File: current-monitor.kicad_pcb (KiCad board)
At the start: 2 copper layers, 91 parts, among them J103 USB-MICROB, J501 JTAG, U201 AD8429A, U202 LM833, U203 TL032C, U301 INA826, U401 LM27313, U402 LTC3260MSE, U403 MAX6070, U501 K22F-64LQFP, U601 TL032C

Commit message: more layout
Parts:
- added C303: C, libs:SMD-2012, F.Cu at (112.4, 86.0)
- added C304: C, libs:SMD-2012, F.Cu at (116.0, 89.6)
- added C305: C, libs:SMD-2012, F.Cu at (132.8, 88.6)
- added C603: 4n, libs:SMD-2012, F.Cu at (132.8, 79.8)
- added D201: BAS40-04, libs:SOT-23, F.Cu at (128.4, 84.2)
- added D301: BAS40-04, libs:SOT-23, F.Cu at (128.4, 88.6)
- added D601: BAS40-04, libs:SOT-23, F.Cu at (126.8, 79.8)
- added R304: Rs, libs:SMD-1608, F.Cu at (110.4, 88.6)
- added R305: Rs, libs:SMD-1608, F.Cu at (113.4, 88.6)
- added R306: R, libs:SMD-1608, F.Cu at (131.0, 88.4)
- moved R401 131.8 mm to (140.6, 102.0)
- moved R409 129.1 mm to (137.6, 103.6), turned to 270 degrees
- moved R408 127.1 mm to (140.6, 103.6), turned to 270 degrees
- moved C404 122.0 mm to (139.0, 112.6)
- moved C408 122.0 mm to (133.7, 105.4)
- moved C409 122.0 mm to (141.2, 109.6)
- moved C405 122.0 mm to (131.8, 112.6)
- moved C407 122.0 mm to (137.1, 105.4)
- moved C410 122.0 mm to (129.6, 109.6)
- moved R404 122.0 mm to (140.6, 107.0)
- moved R405 122.0 mm to (140.6, 105.4)
- moved R406 122.0 mm to (129.4, 105.4)
- moved R407 122.0 mm to (129.4, 107.0)
- moved R410 122.0 mm to (130.8, 103.6)
- moved U402 122.0 mm to (135.4, 108.6)
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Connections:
- net Net-(C207-Pad2) renamed /Current Sense Fine Range/FINE_UNCLAMPED
- net Net-(R601-Pad1) renamed /Sense Voltage/VOLTAGE_RAW
- U202 pad 5: (no net) -> Net-(C303-Pad1)
- U202 pad 6: (no net) -> /Current Sense Coarse Range/COARSE_UNCLAMPED
- U202 pad 7: (no net) -> /Current Sense Coarse Range/COARSE_UNCLAMPED
- U301 pad 7: /Current Sense Coarse Range/SENSE_COARSE -> Net-(R304-Pad1)
- U501 pad 10: /Current Sense Coarse Range/SENSE_COARSE -> (no net)
- U501 pad 11: /MCU/SENSE_VOLTAGE -> /Current Sense Fine Range/SENSE_FINE
- U501 pad 12: (no net) -> /Current Sense Coarse Range/SENSE_COARSE
- U501 pad 9: /Current Sense Fine Range/SENSE_FINE -> /MCU/SENSE_VOLTAGE
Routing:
- net /Current Sense Fine Range/REF_ADJUST: track 0.00 -> 26.3 mm
- net SENSE+: track 4.63 -> 28.8 mm, vias 1 -> 0
- net /Current Sense Coarse Range/COARSE_UNCLAMPED: track 0.00 -> 18.6 mm
- net COM: track 51.6 -> 68.8 mm, vias 48 -> 66
- net SENSE-: track 4.18 -> 19.6 mm, vias 1 -> 0
- net /Current Sense Fine Range/REF_FINE: track 5.07 -> 20.5 mm
- net /Current Sense Coarse Range/SENSE_COARSE: track 0.00 -> 15.1 mm
- net /MCU/SENSE_VOLTAGE: track 1.60 -> 16.5 mm
- net /Current Sense Fine Range/FINE_UNCLAMPED: track 5.99 -> 20.3 mm
- net /Current Sense Coarse Range/REF_COARSE: track 0.00 -> 13.6 mm
- net +3.00V: track 5.69 -> 18.0 mm
- net Net-(R304-Pad1): track 0.00 -> 10.5 mm
- net /Current Sense Fine Range/SENSE_FINE: track 1.60 -> 11.9 mm
- net Net-(R205-Pad1): track 0.00 -> 10.2 mm
- net +3V3: track 0.00 -> 9.16 mm
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- added copper zone on F.Cu, net +5V
- added copper zone on F.Cu, net /Power Supply/+Vs_UNREG
- added copper zone on F.Cu, net Net-(C402-Pad2)
- added copper zone on F.Cu, net Net-(D401-PadA)

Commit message: more layout
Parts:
- added D101: MMBZ15VALT1G, libs:SOT-23, F.Cu at (84.2, 85.0)
- added Y501: 4MHz, libs:OSC3225, F.Cu at (154.8, 87.4)
- moved S501 91.7 mm to (141.3, 94.3)
- moved J501 74.7 mm to (149.6, 95.2)
- moved R501 63.6 mm to (156.2, 82.8), turned to 270 degrees
- moved C510 63.6 mm to (156.2, 84.4)
- moved C413 23.6 mm to (122.8, 109.0), turned to 270 degrees
- moved C412 22.5 mm to (119.0, 111.4), turned to 0 degrees
- moved U403 20.6 mm to (122.2, 111.4), turned to 270 degrees
- moved C411 17.1 mm to (122.8, 113.8), turned to 270 degrees
- moved C404 10.0 mm to (141.5, 102.9), turned to 90 degrees
- moved C405 9.99 mm to (141.5, 110.1), turned to 90 degrees
- moved R401 9.75 mm to (130.9, 101.3), turned to 180 degrees
- moved C409 9.31 mm to (138.5, 100.7), turned to 180 degrees
- moved C410 9.27 mm to (138.5, 112.3), turned to 180 degrees
- moved C101 9.14 mm to (88.0, 80.6), turned to 180 degrees
- moved C102 9.02 mm to (88.0, 89.4), turned to 0 degrees
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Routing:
- net +5V: track 5.47 -> 67.6 mm, vias 0 -> 5
- net +3.00V: track 18.0 -> 45.5 mm
- net COM: track 68.8 -> 87.5 mm, vias 66 -> 86
- net /MCU/SWD_CLK: track 0.00 -> 17.7 mm
- net /MCU/SWD_DIO: track 0.00 -> 14.7 mm
- net /MCU/UART_TX: track 0.00 -> 12.8 mm
- net /MCU/UART_RX: track 0.00 -> 12.1 mm
- net +3V3: track 9.16 -> 19.6 mm, vias 0 -> 11
- net Net-(C502-Pad1): track 0.00 -> 7.19 mm
- net Net-(C501-Pad1): track 0.00 -> 6.33 mm
- net /MCU/~RESET: track 0.00 -> 5.61 mm
- net Net-(R408-Pad2): track 1.45 -> 2.85 mm
- net /Current Sense Fine Range/REF_ADJUST: track 26.3 -> 27.0 mm, vias 0 -> 2
- added copper zone on In2.Cu, net +3V3
- added copper zone on In2.Cu, net +5V
- added copper zone on In2.Cu, net +Vs
- added copper zone on In2.Cu, net -Vs
- added copper zone on B.Cu, net COM
- added copper zone on F.Cu, net COM
- added copper zone on In1.Cu, net COM
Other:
- board outline added: 100 x 50 mm
- copper layers 2 -> 4
- net class Default: clearance 0.2 -> 0.199
- net class Power: clearance 0.2 -> 0.199
- rule trace_clearance: 0.2 -> 0.199

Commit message: more layout
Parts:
- added C511: 1u, libs:SMD-2012, F.Cu at (135.8, 86.2)
- added R502: 33, libs:SMD-1608, F.Cu at (143.4, 72.2)
- added R503: 33, libs:SMD-1608, F.Cu at (143.4, 73.8)
- moved R401 17.3 mm to (148.2, 100.8), turned to 90 degrees
- moved FB501 2.00 mm to (136.0, 88.0)
- moved S501 1.03 mm to (140.8, 95.2)
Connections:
- S501 pad 1: COM -> (no net)
- S501 pad 2: (no net) -> COM
- S501 pad 3: /MCU/~RESET -> (no net)
- S501 pad 4: (no net) -> /MCU/~RESET
- U501 pad 5: /MCU/USB_DP -> Net-(R502-Pad2)
- U501 pad 6: /MCU/USB_DM -> Net-(R503-Pad2)
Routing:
- net /MCU/VS_ENABLE: track 3.17 -> 50.7 mm, vias 2 -> 5
- net /MCU/USB_DM: track 0.00 -> 40.4 mm
- net /MCU/USB_DP: track 0.00 -> 40.3 mm
- net /MCU/~RESET: track 5.61 -> 25.1 mm, vias 0 -> 3
- net +3.00V: track 45.5 -> 60.0 mm
- net /Power Supply/+Vs_UNREG: track 3.32 -> 16.4 mm
- net Net-(R502-Pad2): track 0.00 -> 9.24 mm
- net Net-(R503-Pad2): track 0.00 -> 8.18 mm
- net Net-(R408-Pad2): track 2.85 -> 8.91 mm, vias 1 -> 3
- net Net-(R410-Pad1): track 1.94 -> 5.20 mm, vias 1 -> 2
- net COM: track 87.5 -> 90.7 mm, vias 86 -> 89
- net Net-(C504-Pad1): track 4.86 -> 6.86 mm
- net +3V3: track 19.6 -> 21.6 mm, vias 11 -> 13

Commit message: renumber pcb
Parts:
- added K201: RELAY-DPDT-EE2-SPLIT, libs:RELAY-EE2-NU, F.Cu at (82.0, 143.0)
- added K202: RELAY-DPDT-EE2-SPLIT, libs:RELAY-EE2-NU, F.Cu at (82.0, 132.0)
- added K203: RELAY-DPDT-EE2-SPLIT, libs:RELAY-EE2-NU, F.Cu at (82.0, 165.0)
- added K204: RELAY-DPDT-EE2-SPLIT, libs:RELAY-EE2-NU, F.Cu at (82.0, 154.0)
- added Q201: DRDC3105E6, libs:SOT-23-6, F.Cu at (106.0, 135.0)
- added Q202: DRDC3105E6, libs:SOT-23-6, F.Cu at (102.0, 135.0)
- added Q203: NMOS, libs:SOT-23-FET, F.Cu at (149.7, 148.7)
- added Q204: NMOS, libs:SOT-23-FET, F.Cu at (157.6, 148.7)
- added Q205: NMOS, libs:SOT-23-FET, F.Cu at (153.7, 148.7)
- added R202: 470k 0.05%, libs:SMD-1608, F.Cu at (172.9, 138.2)
- added R203: 470k 0.05%, libs:SMD-1608, F.Cu at (154.0, 154.0)
- added R204: 470k 0.05%, libs:SMD-1608, F.Cu at (172.9, 131.4)
- added R205: Rs, libs:SMD-1608, F.Cu at (153.4, 140.5)
- added R206: 16k 0.05%, libs:SMD-1608, F.Cu at (156.0, 154.0)
- added R207: Rs, libs:SMD-1608, F.Cu at (156.6, 140.8)
- added R208: 150 0.05%, libs:SMD-1608, F.Cu at (152.0, 154.0)
- added R209: Rs, libs:SMD-1608, F.Cu at (150.2, 140.5)
- moved R601 1.60 mm to (143.4, 73.8)
- moved R602 1.60 mm to (143.4, 72.2)
- renumbered C102 to C201, C101 to C202, C201 to C301, C202 to C302, C203 to C303, C204 to C304, C205 to C305, C206 to C306, C212 to C307, C207 to C308, C208 to C309, C209 to C310, C215 to C311, C210 to C312, C301 to C401, C302 to C402, C303 to C403, C304 to C404, C213 to C405, C214 to C406, C306 to C407, C305 to C408, C601 to C501, C602 to C502, C603 to C503, C501 to C601, C502 to C602, C511 to C603, C503 to C604, C504 to C605, C505 to C606, C506 to C607, C507 to C608, C508 to C609, C510 to C610, C509 to C611, C401 to C701, C411 to C702, C412 to C703, C402 to C704, C413 to C705, C403 to C706, C404 to C707, C405 to C708, C406 to C709, C407 to C710, C408 to C711, C409 to C712, C410 to C713, D101 to D201, D201 to D301, D301 to D401, D601 to D501, D401 to D701, FB501 to FB601, J103 to J601, J501 to J602, L401 to L701, R101 to R201, R201 to R301, R202 to R302, R203 to R303, R204 to R304, R205 to R305, R206 to R306, R210 to R307, R211 to R308, R207 to R309, R208 to R310, R212 to R311, R213 to R312, R209 to R313, R301 to R401, R304 to R402, R305 to R403, R302 to R404, R303 to R405, R306 to R406, R603 to R501, R604 to R502, R601 to R503, R602 to R504, R502 to R601, R503 to R602, R501 to R603, R401 to R701, R402 to R702, R403 to R703, R408 to R704, R409 to R705, R410 to R706, R404 to R707, R405 to R708, R406 to R709, R407 to R710, S501 to S601, U201 to U301, U203 to U302, U202 to U303, U301 to U401, U601 to U501, U501 to U601, U401 to U701, U403 to U702, U402 to U703, Y501 to Y601
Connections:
- net Net-(C402-Pad2) renamed /Power Supply/DC_FB
- net Net-(C406-Pad1) renamed /Power Supply/PUMP+
- net Net-(C406-Pad2) renamed /Power Supply/PUMP-
- net Net-(D401-PadA) renamed /Power Supply/DC_SW
- C201 pad 1: SENSE+ -> Net-(C201-Pad1)
- C202 pad 1: SENSE- -> Net-(C202-Pad1)
- D201 pad 1: SENSE+ -> Net-(C201-Pad1)
- D201 pad 2: SENSE- -> Net-(C202-Pad1)
- R601 pad 1: /MCU/USB_DP -> /MCU/USB_DM
- R601 pad 2: Net-(R502-Pad2) (its old number) -> Net-(R601-Pad2)
- R602 pad 1: /MCU/USB_DM -> /MCU/USB_DP
- R602 pad 2: Net-(R503-Pad2) -> Net-(R602-Pad2)
- U601 pad 5: Net-(R502-Pad2) (its old number) -> Net-(R602-Pad2)
- U601 pad 50: (no net) -> /In/Out, Shunt, Calibration/RELAY_INOUT_SHORT
- U601 pad 51: (no net) -> /In/Out, Shunt, Calibration/RELAY_CALIBRATE
- U601 pad 52: (no net) -> /In/Out, Shunt, Calibration/CALIBRATE_5V
- U601 pad 53: (no net) -> /In/Out, Shunt, Calibration/CALIBRATE_3V
- U601 pad 54: (no net) -> /In/Out, Shunt, Calibration/CALIBRATE_30mA
- U601 pad 55: (no net) -> /In/Out, Shunt, Calibration/CALIBRATE_300uA
- U601 pad 56: (no net) -> /In/Out, Shunt, Calibration/CALIBRATE_3uA
- U601 pad 6: Net-(R503-Pad2) -> Net-(R601-Pad2)
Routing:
- net Net-(R602-Pad2): track 0.00 -> 9.24 mm
- net Net-(R502-Pad2) (its old number): track 9.24 -> 0.00 mm
- net Net-(R601-Pad2): track 0.00 -> 8.18 mm
- net Net-(R503-Pad2): track 8.18 -> 0.00 mm
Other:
- board size 100 x 50 mm -> 100 x 70 mm

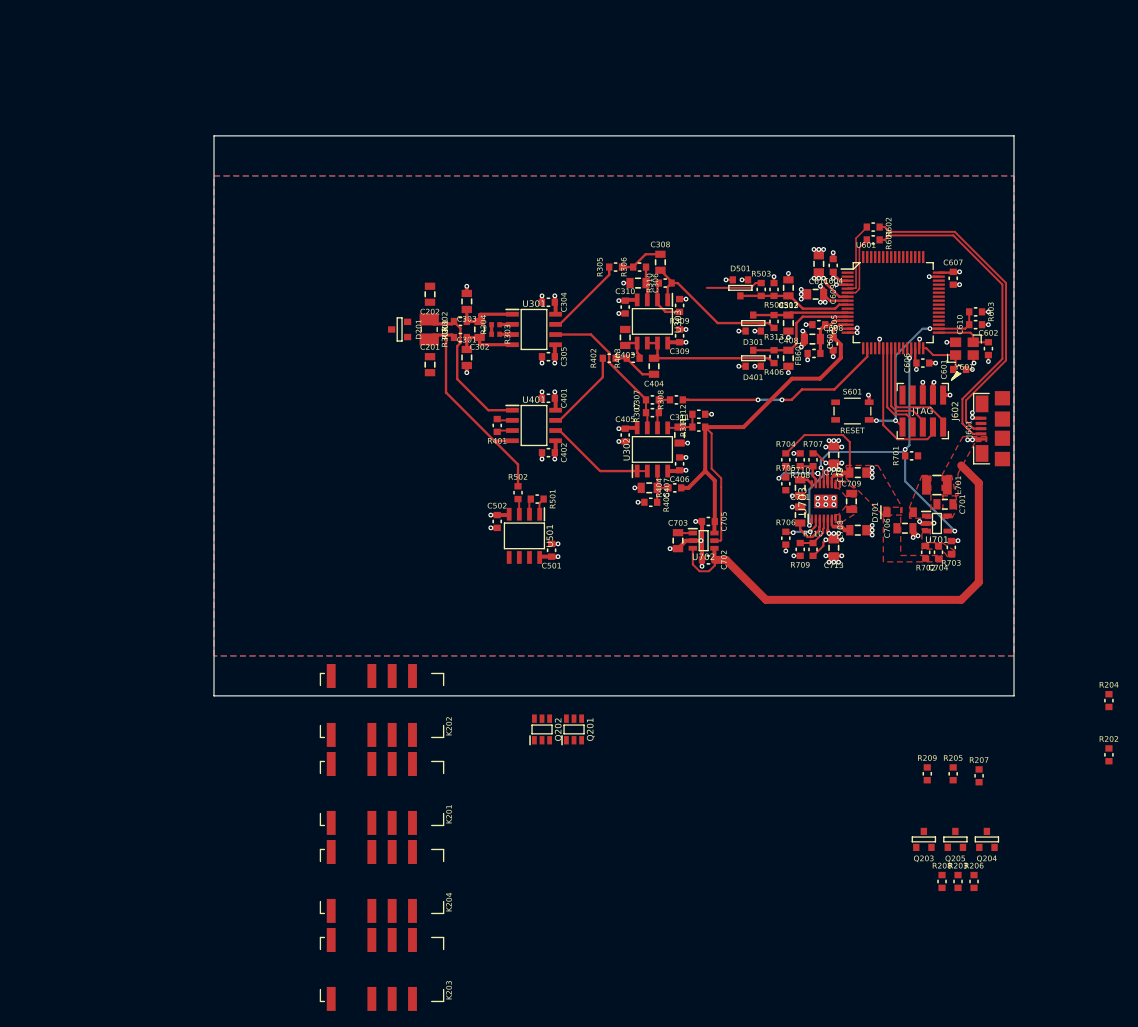
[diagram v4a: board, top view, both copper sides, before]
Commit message: use screw terminals
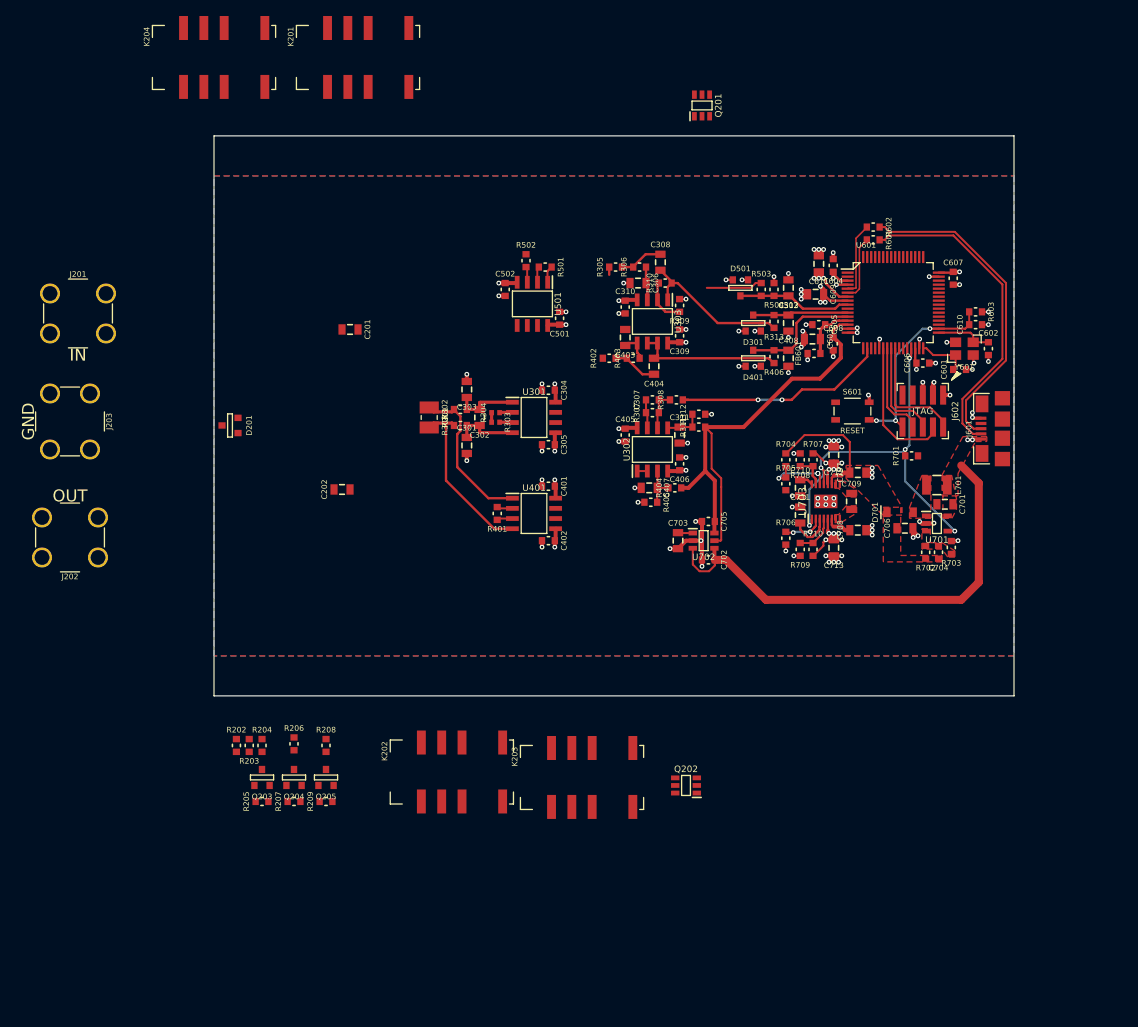
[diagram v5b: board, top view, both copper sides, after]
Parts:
- added J201: IN, libs:SCREW-TERMINAL-7050, F.Cu at (44.0, 83.0)
- added J202: OUT, libs:SCREW-TERMINAL-7050, F.Cu at (43.0, 111.0)
- added J203: GND, libs:SCREW-TERMINAL-7050, F.Cu at (43.0, 96.5)
- moved R202 109.1 mm to (63.8, 137.0)
- moved R204 106.0 mm to (67.0, 137.0)
- moved K204 105.1 mm to (61.0, 51.0), turned to 180 degrees
- moved K201 92.0 mm to (79.0, 51.0), turned to 180 degrees
- moved R203 90.2 mm to (65.4, 137.0), turned to 180 degrees
- moved Q204 87.0 mm to (71.0, 141.0)
- moved R206 86.7 mm to (71.0, 136.8)
- moved R205 86.5 mm to (67.0, 144.0), turned to 90 degrees
- moved R207 85.7 mm to (71.0, 144.0), turned to 90 degrees
- moved Q203 83.1 mm to (67.0, 141.0)
- moved Q201 79.6 mm to (122.0, 57.0)
- moved Q205 79.1 mm to (75.0, 141.0)
- moved R208 78.9 mm to (75.0, 137.0)
- moved R209 75.2 mm to (75.0, 144.0), turned to 90 degrees
- moved K203 34.7 mm to (107.0, 141.0), turned to 180 degrees
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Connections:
- net Net-(C201-Pad1) renamed /In/Out, Shunt, Calibration/IN
- C202 pad 1: Net-(C202-Pad1) -> /In/Out, Shunt, Calibration/OUT
- D201 pad 2: Net-(C202-Pad1) -> /In/Out, Shunt, Calibration/OUT
- K201 pad 5: Net-(C202-Pad1) -> /In/Out, Shunt, Calibration/OUT
- K202 pad 4: +5V -> (no net)
- K202 pad 5: Net-(K202-Pad5) -> (no net)
- K202 pad 8: (no net) -> Net-(K202-Pad8)
- K202 pad 9: (no net) -> +5V
- K203 pad 4: +3.00V -> (no net)
- K203 pad 5: Net-(K202-Pad5) -> (no net)
- K203 pad 8: (no net) -> Net-(K202-Pad8)
- K203 pad 9: (no net) -> +3.00V
- K204 pad 10: Net-(K204-Pad10) -> /In/Out, Shunt, Calibration/OUT
- K204 pad 5: Net-(K202-Pad5) -> Net-(K202-Pad8)
- K204 pad 8: Net-(C202-Pad1) -> Net-(K204-Pad8)
- R202 pad 1: Net-(K204-Pad10) -> Net-(K204-Pad8)
- R206 pad 1: Net-(K204-Pad10) -> Net-(K204-Pad8)
- R208 pad 1: Net-(K204-Pad10) -> Net-(K204-Pad8)
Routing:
- net /Current Sense Fine Range/REF_FINE: track 20.5 -> 5.12 mm
- net /Current Sense Coarse Range/REF_COARSE: track 13.6 -> 1.77 mm
- net Net-(R402-Pad1): track 10.5 -> 0.50 mm
- net Net-(R305-Pad1): track 10.2 -> 1.47 mm
- net SENSE+: track 28.8 -> 21.9 mm

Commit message: checkpoint
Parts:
- removed FB601: FERRITE, libs:SMD-1608
- removed J202: OUT, libs:SCREW-TERMINAL-7050
- removed J203: GND, libs:SCREW-TERMINAL-7050
- removed the K202 at (90.7, 140.3)
- removed K203: RELAY-DPDT-EE2-SPLIT, libs:RELAY-EE2-NU
- removed Q202: DRDC3105E6, libs:SOT-23-6
- removed Q203, Q204, Q205: NMOS, libs:SOT-23-FET
- removed the R205 at (67.0, 144.0)
- removed R209: Rs, libs:SMD-1608
- added C203: 0.1u, libs:SMD-1608, F.Cu at (138.0, 65.4)
- added C204: 0.1u, libs:SMD-1608, F.Cu at (146.6, 71.6)
- added D601: POWER, libs:SMD-1608-LED, F.Cu at (93.8, 79.0)
- added D602: ERROR, libs:SMD-1608-LED, F.Cu at (93.8, 89.0)
- added D603: CAPTURE, libs:SMD-1608-LED, F.Cu at (93.8, 99.0)
- added D604: CALIBRATE, libs:SMD-1608-LED, F.Cu at (93.8, 109.0)
- added F201: FUSE, libs:SMD-1608, F.Cu at (100.6, 63.0)
- added J603: CONN-6, libs:CONN-6-2.54-1.0-PTH, F.Cu at (157.6, 72.5)
- added L601: LCORE, libs:SMD-1608, F.Cu at (136.0, 88.0)
- added L702: LCORE, libs:SMD-1608, F.Cu at (134.2, 97.8)
- added R208: 470k, libs:SMD-1608, F.Cu at (106.0, 76.2)
- added R604: 1k, libs:SMD-1608, F.Cu at (93.8, 82.0)
- added R605: 1k, libs:SMD-1608, F.Cu at (93.8, 92.0)
- added R606: 1k, libs:SMD-1608, F.Cu at (93.8, 102.0)
- added R607: 1k, libs:SMD-1608, F.Cu at (93.8, 112.0)
- added SJ601: SENSE_MCU, libs:SMD-2012, F.Cu at (153.6, 100.0)
- added SJ701: SENSE_ANALOG, libs:SMD-2012, F.Cu at (156.6, 103.6)
- added TP201: SENSE+, libs:TESTPOINT-2.0, F.Cu at (97.8, 82.0)
- added TP202: SENSE-, libs:TESTPOINT-2.0, F.Cu at (107.8, 86.2)
- added TP301: REF_FINE, libs:TESTPOINT-2.0, F.Cu at (123.2, 101.4)
- added TP302: FINE_LOW, libs:TESTPOINT-2.0, F.Cu at (108.4, 99.8)
- added TP303: FINE_UNCLAMPED, libs:TESTPOINT-2.0, F.Cu at (122.2, 85.6)
- added TP304: REF_ADJUST, libs:TESTPOINT-2.0, F.Cu at (141.0, 90.2)
- added TP305: FINE, libs:TESTPOINT-2.0, F.Cu at (125.2, 83.2)
- added TP401: REF_COARSE, libs:TESTPOINT-2.0, F.Cu at (120.8, 114.0)
- added TP402: COARSE_LOW, libs:TESTPOINT-2.0, F.Cu at (108.6, 105.0)
- added TP403: COARSE_UNCLAMPED, libs:TESTPOINT-2.0, F.Cu at (123.4, 95.6)
- added TP404: COARSE, libs:TESTPOINT-2.0, F.Cu at (124.0, 90.4)
- added TP501: VOLTAGE_RAW, libs:TESTPOINT-2.0, F.Cu at (125.0, 75.6)
- added TP502: VOLTAGE, libs:TESTPOINT-2.0, F.Cu at (121.6, 80.4)
- added TP701: +3.00V, libs:TESTPOINT-2.0, F.Cu at (136.6, 96.2)
- added TP702: +Vs_UNREG, libs:TESTPOINT-2.0, F.Cu at (145.4, 102.0)
- added TP703: -Vs_UNREG, libs:TESTPOINT-2.0, F.Cu at (145.8, 114.8)
- added TP704: +Vs, libs:TESTPOINT-2.0, F.Cu at (119.0, 105.4)
- added TP705: -Vs, libs:TESTPOINT-2.0, F.Cu at (98.0, 104.2)
- added U201: FSA1259A, libs:VFSOP-8, F.Cu at (138.6, 63.4)
- added U202: MAX4737EUD, libs:TSSOP-14, F.Cu at (148.8, 68.0)
- J201: value IN -> CONN-3; footprint libs:SCREW-TERMINAL-7050 -> libs:TERM-3-3.5-PTH
- R207: value Rs -> 470k
- moved R206 105.4 mm to (151.4, 64.4), turned to 90 degrees
- moved R202 102.8 mm to (142.8, 71.2), turned to 90 degrees
- moved R203 102.6 mm to (142.8, 69.6), turned to 270 degrees
- moved R204 102.5 mm to (142.8, 68.0), turned to 90 degrees
- moved R205 100.8 mm to (142.8, 66.0), turned to 90 degrees
- moved R207 79.4 mm to (116.4, 78.8), turned to 0 degrees
- moved D201 70.9 mm to (130.3, 75.0), turned to 180 degrees
- moved J201 57.1 mm to (99.8, 71.0), turned to 270 degrees
- moved K201 53.5 mm to (111.9, 67.6), turned to 0 degrees
- moved K202 51.6 mm to (127.9, 67.6), turned to 0 degrees
- moved C202 42.2 mm to (107.8, 76.2), turned to 0 degrees
- moved C201 37.1 mm to (114.6, 78.8), turned to 0 degrees
- moved R502 30.8 mm to (112.4, 104.6), turned to 90 degrees
- moved C501 30.3 mm to (117.2, 111.0)
- moved C502 30.3 mm to (110.4, 107.4)
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- renumbered K204 to K201, K201 to K202, R206 to R205, R208 to R206
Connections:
- net Net-(R402-Pad1) renamed /Current Sense Coarse Range/COARSE_UNFILTERED
- C609 pad 1: +5V -> /MCU/5V_MCU
- C701 pad 1: +5V -> /Power Supply/5V_ANALOG
- C702 pad 1: +5V -> Net-(C702-Pad1)
- J201 pad 1: /In/Out, Shunt, Calibration/IN -> Net-(F201-Pad2)
- K202 pad 4: /In/Out, Shunt, Calibration/IN -> (no net)
- K202 pad 5: /In/Out, Shunt, Calibration/OUT -> (no net)
- K202 pad 8: (no net) -> /In/Out, Shunt, Calibration/IN
- K202 pad 9: (no net) -> /In/Out, Shunt, Calibration/OUT
- L701 pad 1: +5V -> /Power Supply/5V_ANALOG
- R207 pad 1: /In/Out, Shunt, Calibration/CALIBRATE_300uA -> /In/Out, Shunt, Calibration/IN
- U501 pad 5: (no net) -> COM
- U501 pad 6: (no net) -> Net-(U501-Pad6)
- U501 pad 7: (no net) -> Net-(U501-Pad6)
- U601 pad 43: (no net) -> /MCU/GPIO0
- U601 pad 44: (no net) -> /MCU/GPIO1
- U601 pad 45: (no net) -> /MCU/GPIO2
- U601 pad 46: (no net) -> /MCU/GPIO3
- U601 pad 49: (no net) -> /MCU/GPIO4
- U601 pad 50: /In/Out, Shunt, Calibration/RELAY_INOUT_SHORT -> (no net)
- U601 pad 51: /In/Out, Shunt, Calibration/RELAY_CALIBRATE -> (no net)
- U601 pad 52: /In/Out, Shunt, Calibration/CALIBRATE_5V -> (no net)
- U601 pad 53: /In/Out, Shunt, Calibration/CALIBRATE_3V -> /MCU/LED_CALIBRATE
- U601 pad 54: /In/Out, Shunt, Calibration/CALIBRATE_30mA -> /MCU/LED_CAPTURE
- U601 pad 55: /In/Out, Shunt, Calibration/CALIBRATE_300uA -> /MCU/LED_ERROR
- U601 pad 56: /In/Out, Shunt, Calibration/CALIBRATE_3uA -> /MCU/LED_POWER
- U601 pad 57: (no net) -> /In/Out, Shunt, Calibration/RELAY_INOUT_SHORT
- U601 pad 58: (no net) -> /In/Out, Shunt, Calibration/RELAY_CALIBRATE
- U601 pad 59: (no net) -> /In/Out, Shunt, Calibration/CALIBRATE_3V
- U601 pad 60: (no net) -> /In/Out, Shunt, Calibration/CALIBRATE_5V
- U601 pad 61: (no net) -> /In/Out, Shunt, Calibration/CALIBRATE_30mA_2
- U601 pad 62: (no net) -> /In/Out, Shunt, Calibration/CALIBRATE_300uA
- U601 pad 63: (no net) -> /In/Out, Shunt, Calibration/CALIBRATE_3uA
- U601 pad 64: (no net) -> /In/Out, Shunt, Calibration/CALIBRATE_30mA
- U601 pad 8: +5V -> /MCU/5V_MCU
- U701 pad 5: +5V -> /Power Supply/5V_ANALOG
- U702 pad 3: +5V -> Net-(C702-Pad1)
- U702 pad 4: +5V -> Net-(C702-Pad1)
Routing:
- net /MCU/LED_POWER: track 0.00 -> 103.6 mm, vias 0 -> 2
- net /MCU/LED_ERROR: track 0.00 -> 95.4 mm, vias 0 -> 2
- net /MCU/LED_CAPTURE: track 0.00 -> 86.6 mm, vias 0 -> 2
- net +3V3: track 21.6 -> 107.7 mm
- net -Vs: track 22.1 -> 103.3 mm
- net +5V: track 67.6 -> 147.3 mm, vias 5 -> 8
- net /MCU/LED_CALIBRATE: track 0.00 -> 79.2 mm, vias 0 -> 2
- net SENSE+: track 21.9 -> 85.4 mm, vias 0 -> 2
- net +Vs: track 22.9 -> 84.5 mm
- net /In/Out, Shunt, Calibration/IN: track 0.00 -> 59.2 mm, vias 0 -> 3
- net /In/Out, Shunt, Calibration/OUT: track 0.00 -> 58.1 mm, vias 0 -> 1
- net SENSE-: track 19.6 -> 61.4 mm, vias 0 -> 2
- net Net-(K201-Pad8): track 0.00 -> 41.7 mm
- net /In/Out, Shunt, Calibration/CALIBRATE_5V: track 0.00 -> 36.1 mm
- net /In/Out, Shunt, Calibration/RELAY_CALIBRATE: track 0.00 -> 34.0 mm, vias 0 -> 2
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- added copper zone on F.Cu, net /Power Supply/5V_ANALOG
- removed copper zone on In2.Cu, net +3V3
- removed copper zone on F.Cu, net +5V
- removed copper zone on In2.Cu, net +5V
- removed copper zone on In2.Cu, net +Vs
- removed copper zone on In2.Cu, net -Vs
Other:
- outline, holes or cut-outs redrawn
